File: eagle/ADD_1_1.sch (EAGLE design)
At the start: 14 parts, among them IC1 74HC283N, X1 In A, X2 In B, X3 Carry, X4 OUT

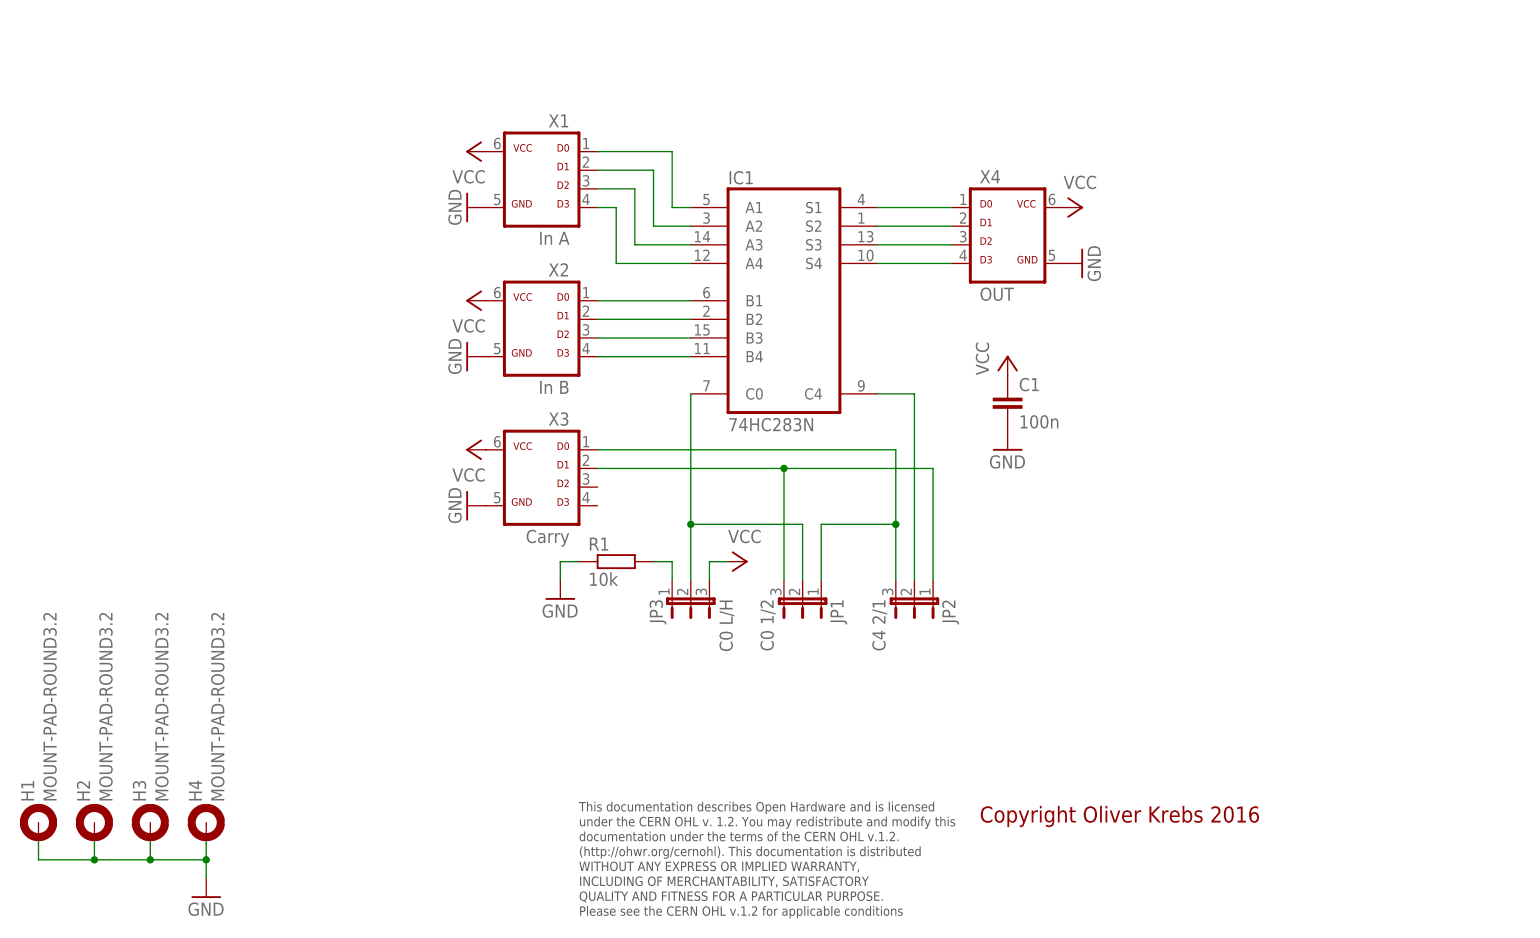
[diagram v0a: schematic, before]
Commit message: Add new tetra-Board and arduino files
Add AMP_1_0, AVC_1_0, D18_1_1, IOP_1_2, MIC_1_0, PIN_1_1, POT_1_0, PWA_1_0, PWR_1_0, RGF 2.0, SOC_2_0, VLT_1_0
Add mex_nano_shield_keyboard, mex_nano_shied_numbers

New arduino projects
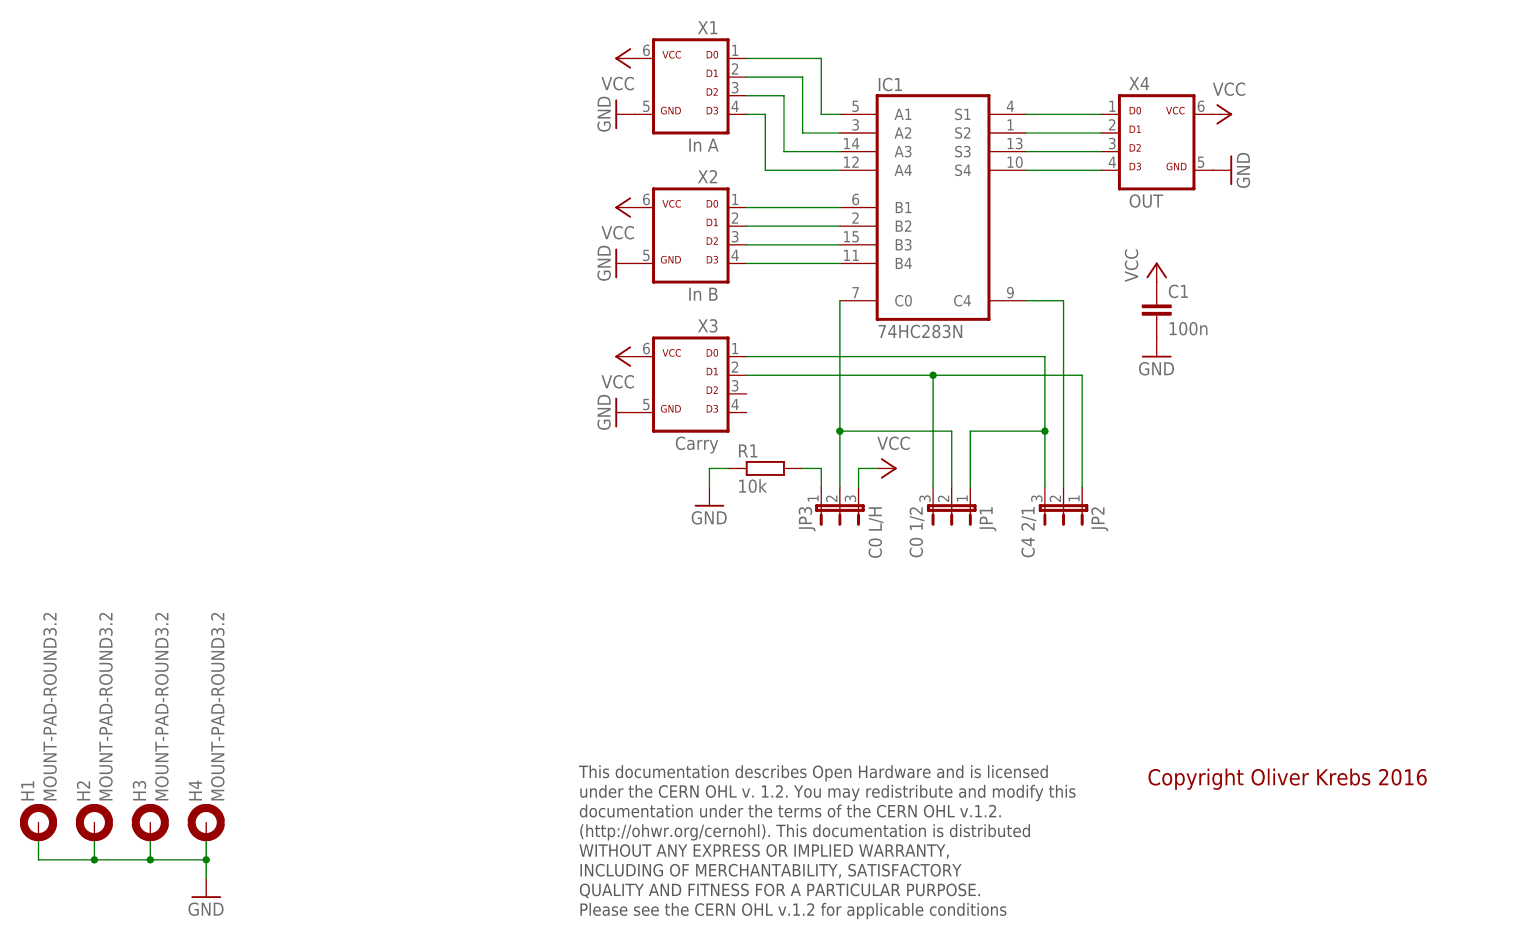
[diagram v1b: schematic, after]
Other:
- moved on the sheet: C1, IC1, JP1, JP2, JP3, R1, X1, X2, X3, X4
